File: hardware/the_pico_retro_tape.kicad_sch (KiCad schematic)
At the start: 11 parts, among them U1 Pico

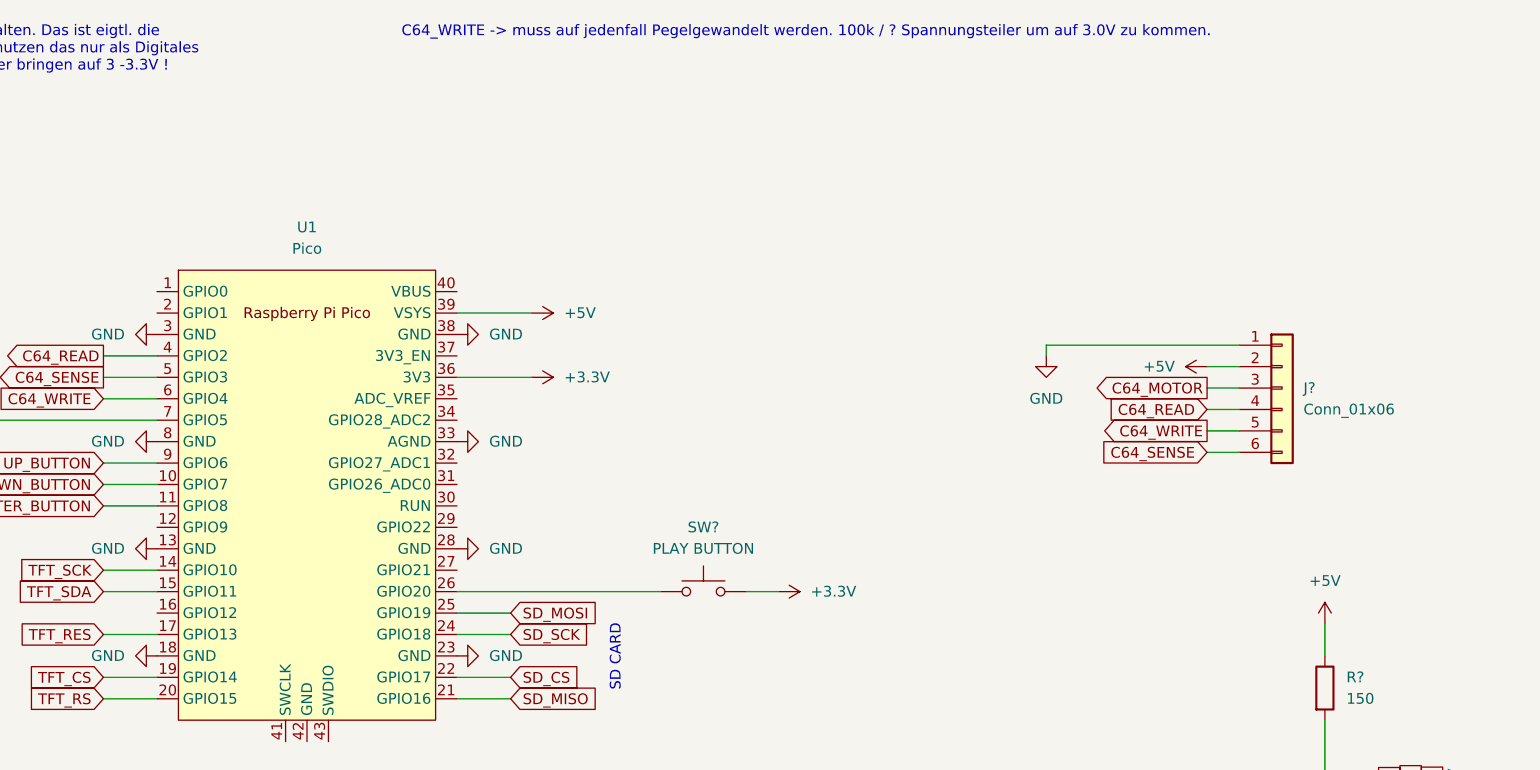
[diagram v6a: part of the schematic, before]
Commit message: hardware: added a transistor for pull the sense signal to ground
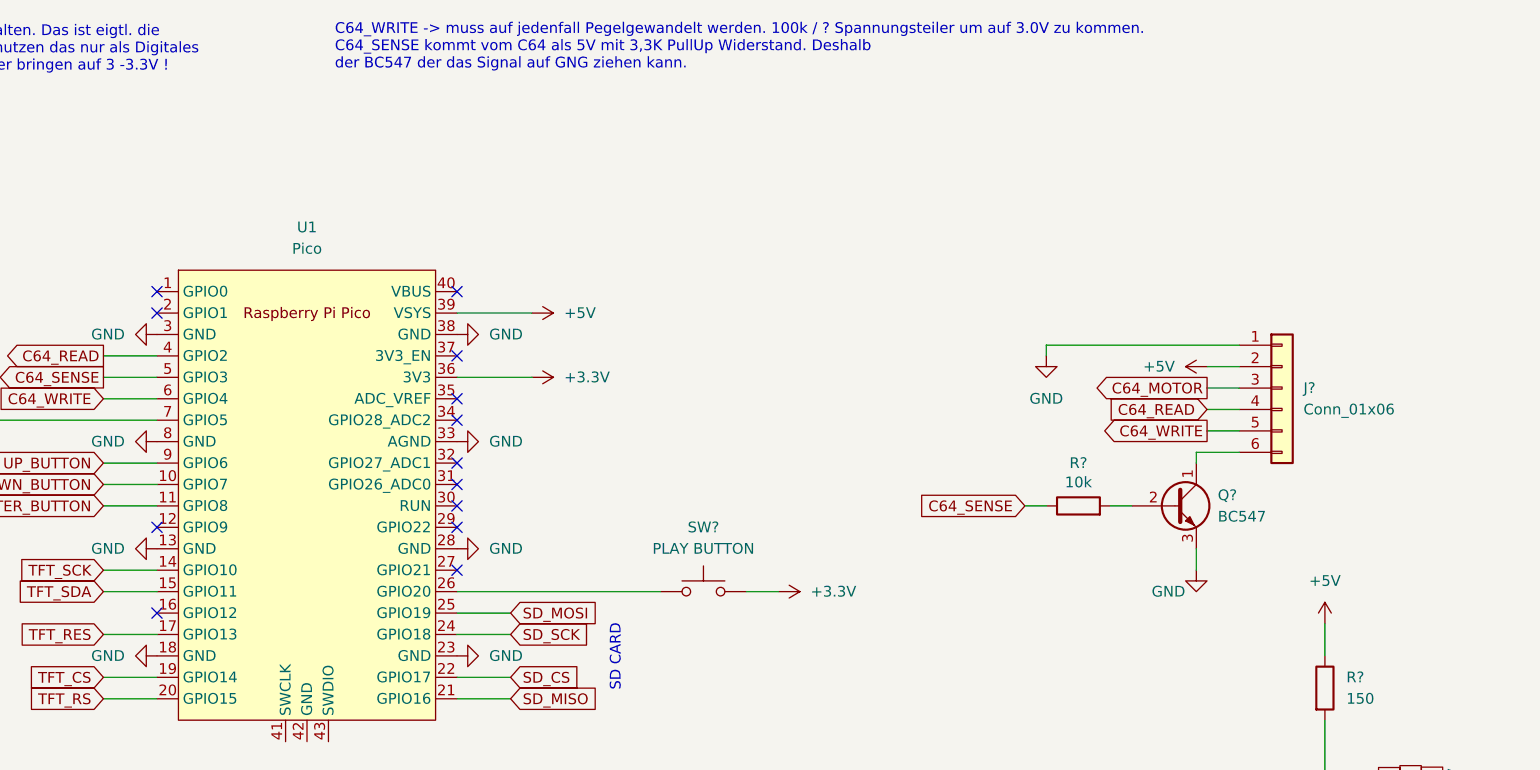
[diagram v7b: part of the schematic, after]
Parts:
- added Q?: BC547, Package_TO_SOT_THT:TO-92_Inline, symbol Transistor_BJT:BC547
- added R?: 10k, symbol Device:R
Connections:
- net C64_SENSE: now also R?.1; no longer J?.6 (Pin_6)
- net GND: now also Q?.3 (E)
- new net: Q?.2 (B), R?.2
- new net: J?.6 (Pin_6), Q?.1 (C)
- no-connect marks 1 -> 14
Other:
- note added: "C64_WRITE -> muss auf jedenfall Pegelgewandelt werden. 100k / ? Spannungsteiler um auf 3.0V zu kommen. C64_SENSE kommt vom C64 als 5V mit 3,3K PullUp Widerstand. Deshalb der BC547 der das Signal auf GNG ziehen kann."
- note removed: "C64_WRITE -> muss auf jedenfall Pegelgewandelt werden. 100k / ? Spannungsteiler um auf 3.0V zu kommen."

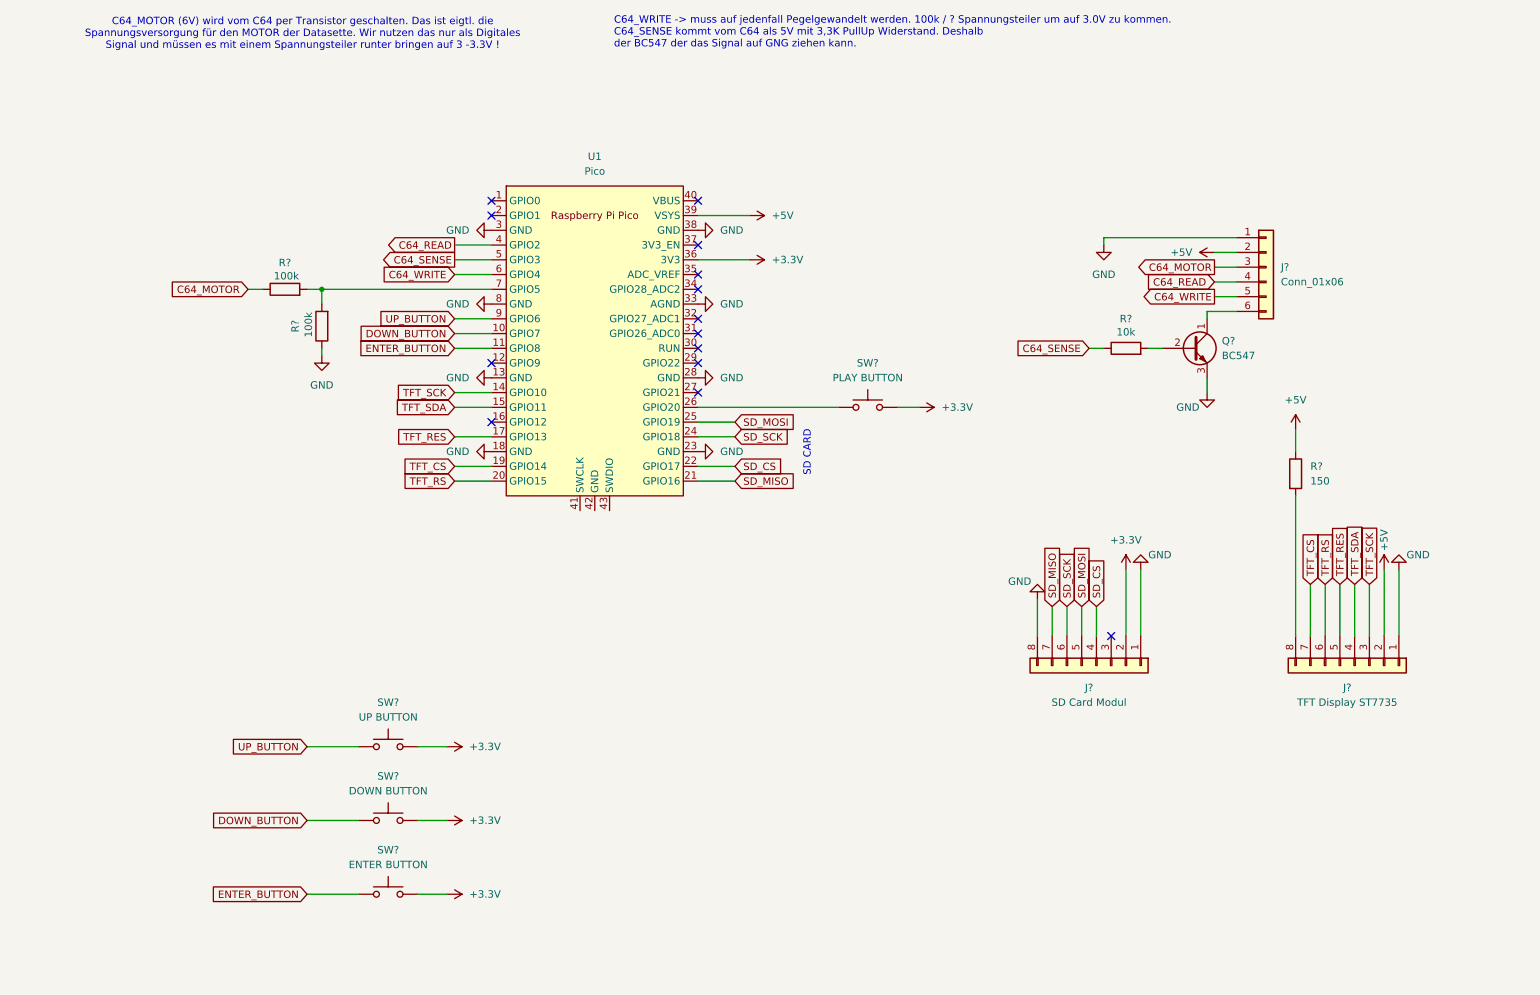
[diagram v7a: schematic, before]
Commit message: fix: update schematic references and properties in the_pico_retro_tape.kicad_sch
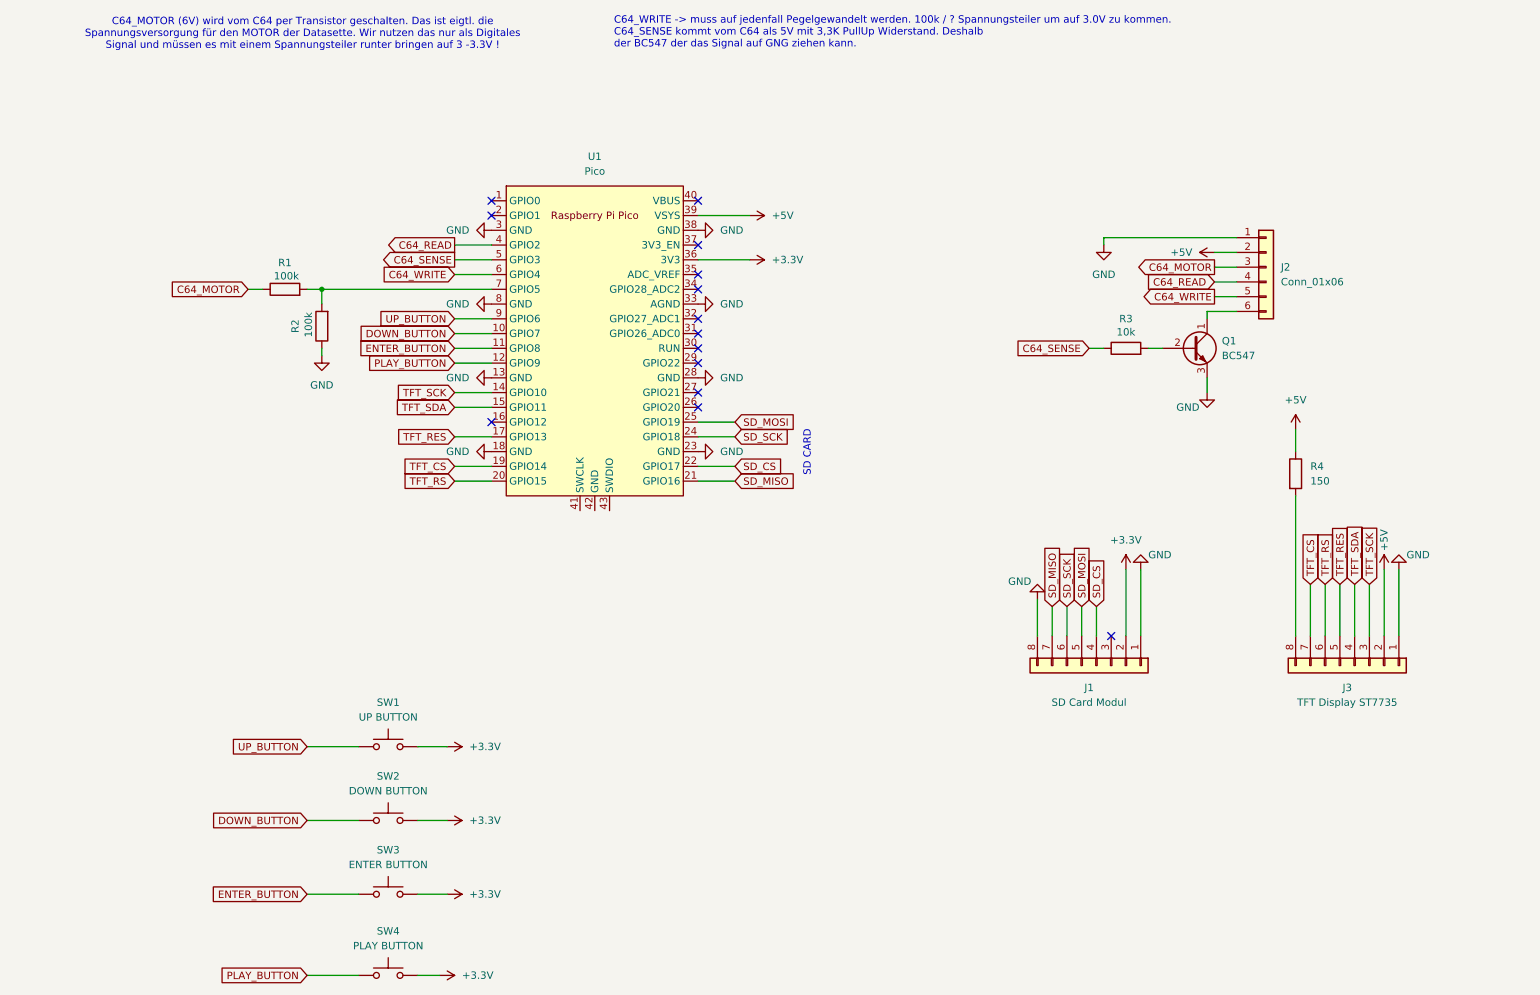
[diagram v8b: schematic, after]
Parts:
- removed SW?: PLAY BUTTON, symbol Switch:SW_Push
- added SW4: PLAY BUTTON, symbol Switch:SW_Push
- gave numbers to parts that had none: 11
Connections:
- net +3.3V: now also SW4.2
- net PLAY_BUTTON: now reaches U1.12 (GPIO9)
- net PLAY_BUTTON: now also SW4.1
